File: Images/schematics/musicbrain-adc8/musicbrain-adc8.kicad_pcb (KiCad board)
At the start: 2 copper layers, 80 x 44 mm, 23 parts, among them J1 BUS, J2 CV IN, U1 AD7606BSTZ, U2 AMS1117-5.0

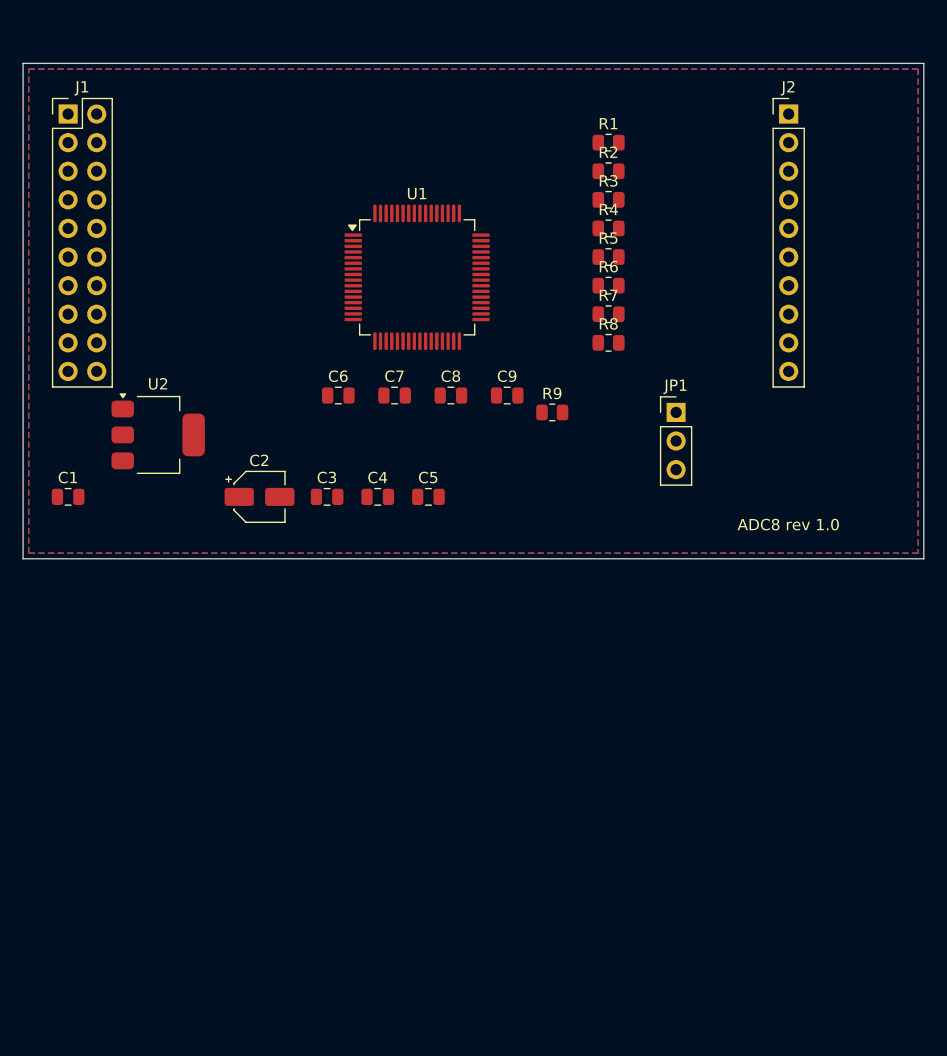
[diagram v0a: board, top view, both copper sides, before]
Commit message: ADC8 v1.1: haakse connectoren + volledige routing (DRC 0/0)
- bord van 80x44 naar 40x80 mm (H=80-standaard); J1 haaks onder,
  J2 haaks boven, gecentreerd boven het slot
- de v1.0-routing liep twee keer vast; de bovenplaat-layout lost het op:
  V1..V8 -> IN1..IN8 (volledige orde-omkering) via Manhattan-routing
  (F.Cu alleen verticalen, B.Cu 8 horizontale lanes op 0,8mm steek),
  westkolom-entries kruisingsvrij met 'diepste entry = oostelijkste
  verticaal', GND-verzamelrail voor de pads tussen de escapes
- ERC 0, netlijst pad-voor-pad geverifieerd, DRC 0/0 met zone-refill

Co-Authored-By: Claude Fable 5 <noreply@anthropic.com>
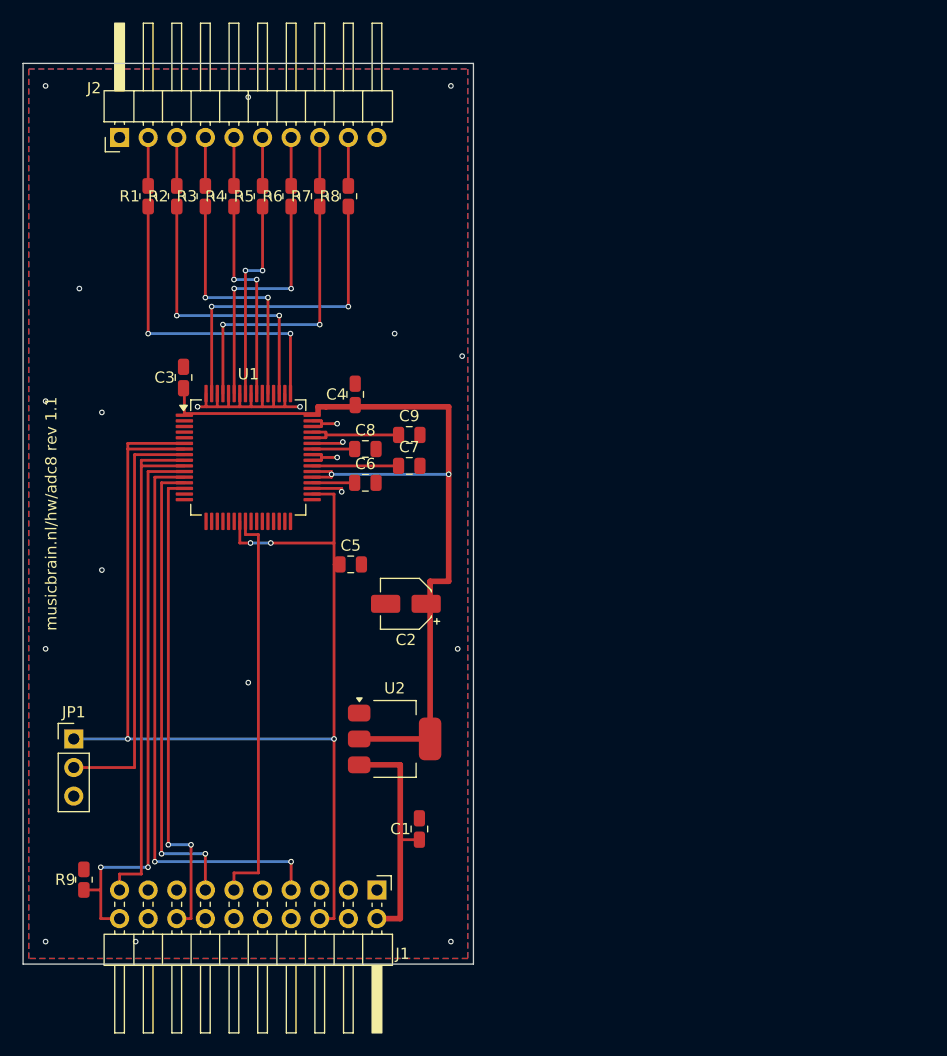
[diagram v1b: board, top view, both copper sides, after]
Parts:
- J1: footprint Connector_PinHeader_2.54mm:PinHeader_2x10_P2.54mm_Vertical -> Connector_PinHeader_2.54mm:PinHeader_2x10_P2.54mm_Horizontal
- J2: footprint Connector_PinHeader_2.54mm:PinHeader_1x10_P2.54mm_Vertical -> Connector_PinHeader_2.54mm:PinHeader_1x10_P2.54mm_Horizontal
- moved J1 74.2 mm to (131.4, 173.4), turned to 270 degrees
- moved JP1 60.9 mm to (104.5, 160.0)
- moved J2 59.5 mm to (108.6, 106.6), turned to 90 degrees
- moved R9 58.8 mm to (105.4, 172.5), turned to 90 degrees
- moved C1 42.9 mm to (135.2, 168.0), turned to 90 degrees
- moved R1 41.2 mm to (111.1, 111.8), turned to 90 degrees
- moved R2 38.4 mm to (113.7, 111.8), turned to 90 degrees
- moved R3 35.8 mm to (116.2, 111.8), turned to 90 degrees
- moved U2 34.2 mm to (133.0, 160.0)
- moved R4 33.4 mm to (118.7, 111.8), turned to 90 degrees
- moved R5 31.2 mm to (121.3, 111.8), turned to 90 degrees
- moved R6 29.3 mm to (123.8, 111.8), turned to 90 degrees
- moved R7 27.7 mm to (126.3, 111.8), turned to 90 degrees
- moved R8 26.5 mm to (128.9, 111.8), turned to 90 degrees
- moved U1 21.9 mm to (120.0, 135.0)
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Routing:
- net +3V3: track 0.00 -> 111.2 mm, vias 0 -> 4
- net +5V: track 0.00 -> 78.7 mm, vias 0 -> 2
- net /SCLK: track 0.00 -> 51.4 mm, vias 0 -> 2
- net /RESET: track 0.00 -> 50.3 mm, vias 0 -> 2
- net /CONVST: track 0.00 -> 47.8 mm
- net /IRQ: track 0.00 -> 42.9 mm, vias 0 -> 2
- net /CS: track 0.00 -> 42.1 mm, vias 0 -> 2
- net /RANGE: track 0.00 -> 37.6 mm
- net /MISO: track 0.00 -> 36.1 mm
- net GND: track 0.00 -> 31.4 mm, vias 0 -> 21
- net Net-(U1-V1): track 0.00 -> 29.3 mm, vias 0 -> 2
- net Net-(U1-V8): track 0.00 -> 28.8 mm, vias 0 -> 2
- net Net-(U1-V2): track 0.00 -> 25.7 mm, vias 0 -> 2
- net Net-(U1-V7): track 0.00 -> 25.2 mm, vias 0 -> 2
- net Net-(U1-V3): track 0.00 -> 22.2 mm, vias 0 -> 2
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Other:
- board size 80 x 44 mm -> 40 x 80 mm
- board text added: "musicbrain.nl/hw/adc8 rev 1.1"
- board text removed: "ADC8 rev 1.0"

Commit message: ADC8 v1.2: recht-toe-bedrading + firmware-remap (DRC 0/0 + fab)
V-omkering eruit: V_k nu recht naar paneeljack (9-k) via een ordebehoudende
F.Cu-waaier (geen B-lanes/vias meer). MbAdc8::read() spiegelt de AD7606-
stream zodat out[0..7] = paneeljack 1..8; jack-contract op J2 ongewijzigd.
ERC 0, netcheck OK, DRC 0/0, fab ververst (JLC-formaat) - bestelbaar.

Co-Authored-By: Claude Fable 5 <noreply@anthropic.com>
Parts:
- moved R1 17.8 mm to (128.9, 111.8)
- moved R8 17.8 mm to (111.1, 111.8)
- moved R2 12.7 mm to (126.3, 111.8)
- moved R7 12.7 mm to (113.7, 111.8)
- moved R3 7.62 mm to (123.8, 111.8)
- moved R6 7.62 mm to (116.2, 111.8)
- moved R4 2.54 mm to (121.3, 111.8)
- moved R5 2.54 mm to (118.7, 111.8)
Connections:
- R1 pad 2: /IN1 -> /IN8
- R2 pad 2: /IN2 -> /IN7
- R3 pad 2: /IN3 -> /IN6
- R4 pad 2: /IN4 -> /IN5
- R5 pad 2: /IN5 -> /IN4
- R6 pad 2: /IN6 -> /IN3
- R7 pad 2: /IN7 -> /IN2
- R8 pad 2: /IN8 -> /IN1
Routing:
- net Net-(U1-V1): track 29.3 -> 21.8 mm, vias 2 -> 0
- net Net-(U1-V8): track 28.8 -> 22.3 mm, vias 2 -> 0
- net Net-(U1-V2): track 25.7 -> 20.2 mm, vias 2 -> 0
- net Net-(U1-V7): track 25.2 -> 20.7 mm, vias 2 -> 0
- net Net-(U1-V3): track 22.2 -> 18.7 mm, vias 2 -> 0
- net Net-(U1-V6): track 21.7 -> 19.2 mm, vias 2 -> 0
- net Net-(U1-V4): track 18.6 -> 17.1 mm, vias 2 -> 0
- net Net-(U1-V5): track 18.1 -> 17.6 mm, vias 2 -> 0
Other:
- board text added: "musicbrain.nl/hw/adc8 rev 1.2"
- board text removed: "musicbrain.nl/hw/adc8 rev 1.1"
